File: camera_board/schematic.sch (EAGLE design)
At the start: 1 part

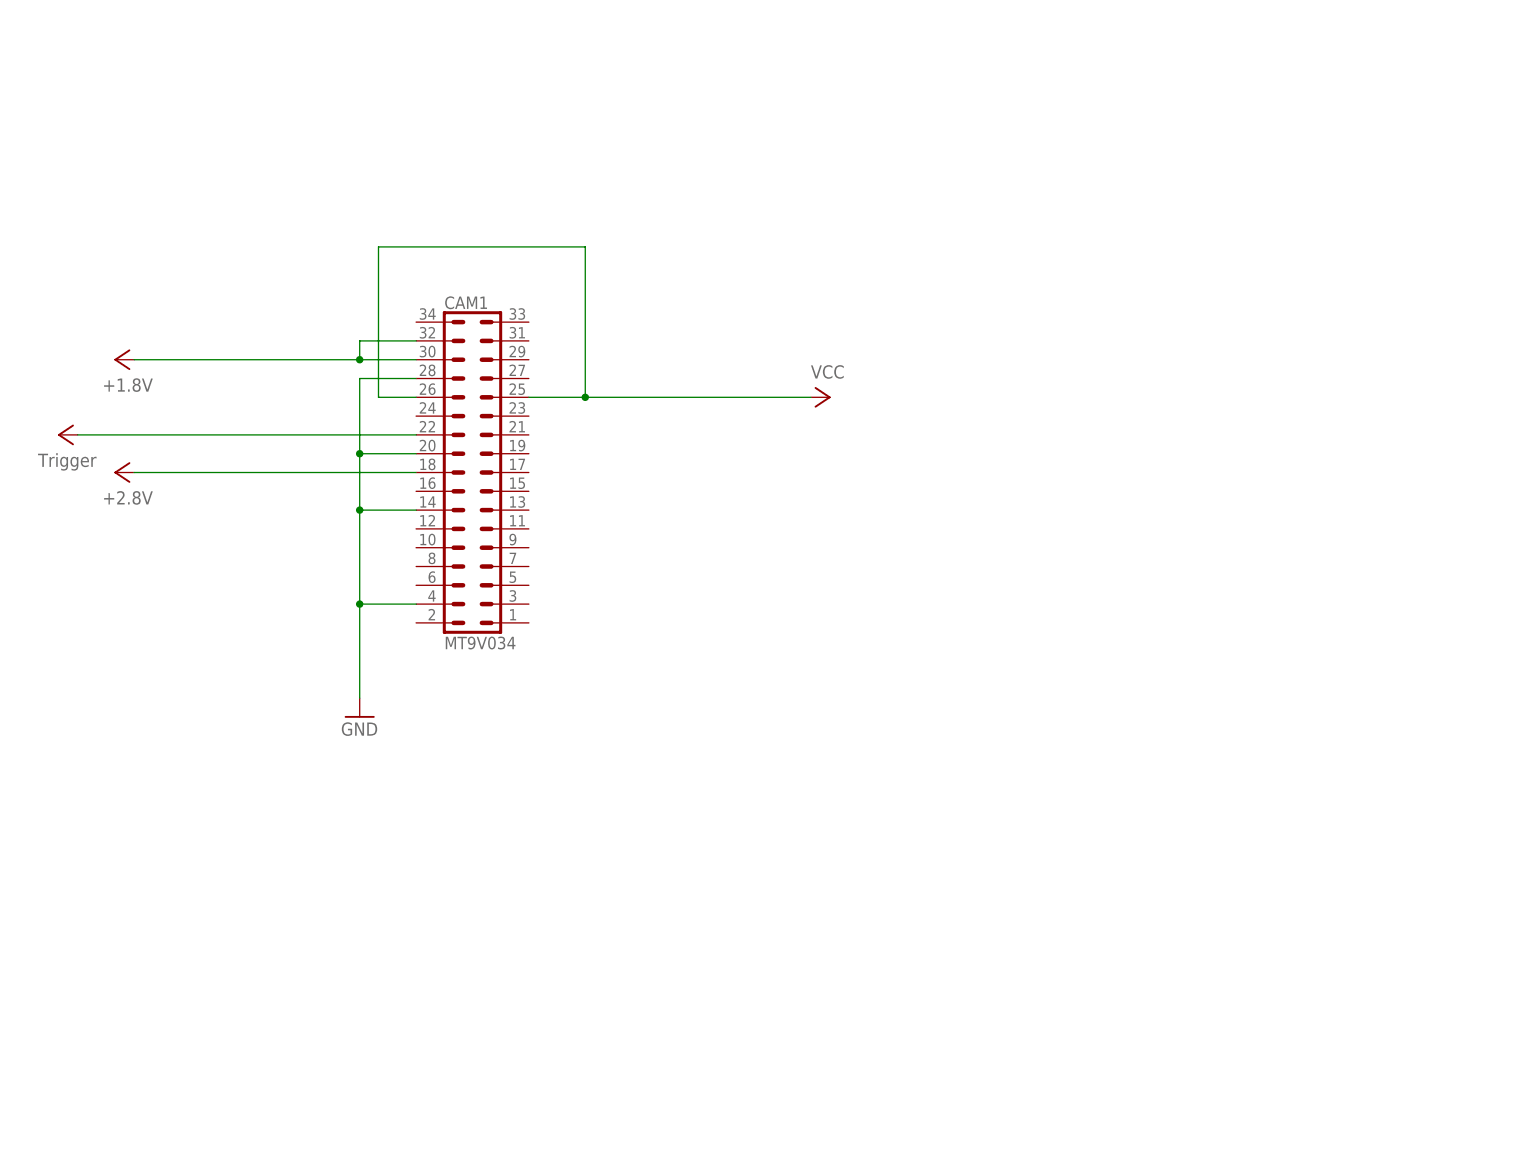
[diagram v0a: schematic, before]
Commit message: Completed Schematic, Started Board
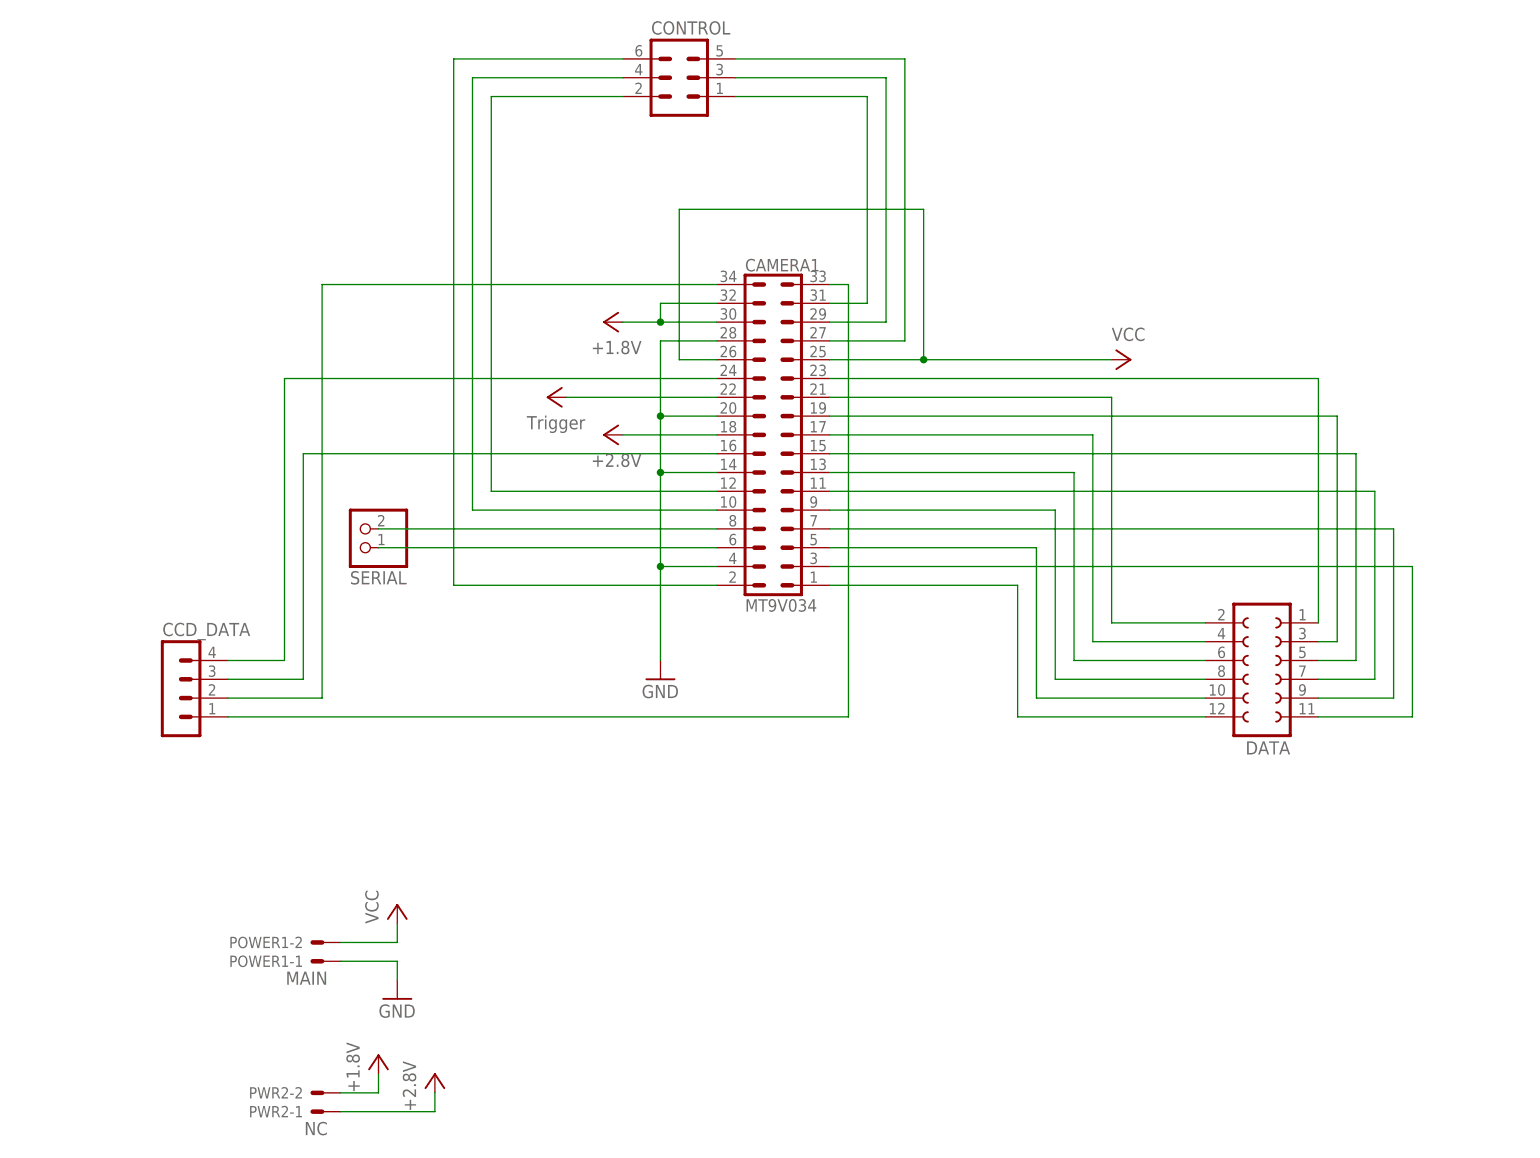
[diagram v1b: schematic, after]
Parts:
- removed CAM1: MT9V034, _hhn_con_pinhead_box_1mm27:PHB_1MM27_2X17_SNT
- added CAMERA1: MT9V034, _hhn_con_pinhead_box_1mm27:PHB_1MM27_2X17_SNT
- added CCD_DATA: (no value), con-lstb:MA04-1
- added CONTROL: (no value), con-lstb:MA03-2
- added DATA: (no value), con-lsta:FE06-2
- added POWER1: MAIN, con-molex:22-23-2021
- added PWR2: NC, con-molex:22-23-2021
- added SERIAL: (no value), pinhead:PINHD-1X2
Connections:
- new net N$1: CAMERA1.23, DATA.1
- new net N$10: CAMERA1.5, DATA.10
- new net N$11: CAMERA1.3, DATA.11
- new net N$12: CAMERA1.1, DATA.12
- new net N$13: CAMERA1.12, CONTROL.2
- new net N$14: CAMERA1.10, CONTROL.4
- new net N$15: CAMERA1.2, CONTROL.6
- new net N$16: CAMERA1.31, CONTROL.1
- new net N$17: CAMERA1.29, CONTROL.3
- new net N$18: CAMERA1.27, CONTROL.5
- new net N$19: CAMERA1.33, CCD_DATA.1
- new net N$2: CAMERA1.21, DATA.2
- new net N$20: CAMERA1.34, CCD_DATA.2
- new net N$21: CAMERA1.16, CCD_DATA.3
- new net N$22: CAMERA1.24, CCD_DATA.4
- new net N$23: CAMERA1.8, SERIAL.2
- new net N$24: CAMERA1.6, SERIAL.1
- new net N$3: CAMERA1.19, DATA.3
- new net N$4: CAMERA1.17, DATA.4
- new net N$5: CAMERA1.15, DATA.5
- new net N$6: CAMERA1.13, DATA.6
- new net N$7: CAMERA1.11, DATA.7
- new net N$8: CAMERA1.9, DATA.8
- new net N$9: CAMERA1.7, DATA.9
- net 1.8V: now also CAMERA1.30, CAMERA1.32, PWR2-2.S; no longer CAM1.30, CAM1.32
- net 2.8V: now also CAMERA1.18, PWR2-1.S; no longer CAM1.18
- net GND: now also CAMERA1.14, CAMERA1.20, CAMERA1.28, CAMERA1.4, POWER1-1.S; no longer CAM1.14, CAM1.20, CAM1.28, CAM1.4
- net TRIGGER: now also CAMERA1.22; no longer CAM1.22
- net VCC: now also CAMERA1.25, CAMERA1.26, POWER1-2.S; no longer CAM1.25, CAM1.26

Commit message: Updated Schematic and Board
I'm debating on removing the ccd_data pin breakout all together - more
to come on this
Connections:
- net N$13: now also CONTROL.6; no longer CONTROL.2
- net N$15: now also CONTROL.2; no longer CONTROL.6
- net N$16: now also CONTROL.5; no longer CONTROL.1
- net N$18: now also CONTROL.1; no longer CONTROL.5
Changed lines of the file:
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@@
 <pinref part="CAMERA1" gate="G$1" pin="12"/>
 <wire x1="116.84" y1="104.14" x2="86.36" y2="104.14" width="0.1524" layer="91"/>
-<wire x1="86.36" y1="104.14" x2="86.36" y2="157.48" width="0.1524" layer="91"/>
-<pinref part="CONTROL" gate="1" pin="2"/>
-<wire x1="86.36" y1="157.48" x2="104.14" y2="157.48" width="0.1524" layer="91"/>
+<wire x1="86.36" y1="104.14" x2="86.36" y2="162.56" width="0.1524" layer="91"/>
+<pinref part="CONTROL" gate="1" pin="6"/>
+<wire x1="86.36" y1="162.56" x2="104.14" y2="162.56" width="0.1524" layer="91"/>
 </segment>
 </net>
@@
 <pinref part="CAMERA1" gate="G$1" pin="2"/>
 <wire x1="116.84" y1="91.44" x2="81.28" y2="91.44" width="0.1524" layer="91"/>
-<wire x1="81.28" y1="91.44" x2="81.28" y2="162.56" width="0.1524" layer="91"/>
-<pinref part="CONTROL" gate="1" pin="6"/>
-<wire x1="81.28" y1="162.56" x2="104.14" y2="162.56" width="0.1524" layer="91"/>
+<wire x1="81.28" y1="91.44" x2="81.28" y2="157.48" width="0.1524" layer="91"/>
+<pinref part="CONTROL" gate="1" pin="2"/>
+<wire x1="81.28" y1="157.48" x2="104.14" y2="157.48" width="0.1524" layer="91"/>
 </segment>
 </net>
@@
 <pinref part="CAMERA1" gate="G$1" pin="31"/>
 <wire x1="132.08" y1="129.54" x2="137.16" y2="129.54" width="0.1524" layer="91"/>
-<wire x1="137.16" y1="129.54" x2="137.16" y2="157.48" width="0.1524" layer="91"/>
-<pinref part="CONTROL" gate="1" pin="1"/>
-<wire x1="137.16" y1="157.48" x2="119.38" y2="157.48" width="0.1524" layer="91"/>
+<wire x1="137.16" y1="129.54" x2="137.16" y2="162.56" width="0.1524" layer="91"/>
+<pinref part="CONTROL" gate="1" pin="5"/>
+<wire x1="119.38" y1="162.56" x2="137.16" y2="162.56" width="0.1524" layer="91"/>
 </segment>
 </net>
@@
 <pinref part="CAMERA1" gate="G$1" pin="27"/>
 <wire x1="132.08" y1="124.46" x2="142.24" y2="124.46" width="0.1524" layer="91"/>
-<wire x1="142.24" y1="124.46" x2="142.24" y2="162.56" width="0.1524" layer="91"/>
-<pinref part="CONTROL" gate="1" pin="5"/>
-<wire x1="142.24" y1="162.56" x2="119.38" y2="162.56" width="0.1524" layer="91"/>
+<wire x1="142.24" y1="124.46" x2="142.24" y2="157.48" width="0.1524" layer="91"/>
+<pinref part="CONTROL" gate="1" pin="1"/>
+<wire x1="119.38" y1="157.48" x2="142.24" y2="157.48" width="0.1524" layer="91"/>
 </segment>
 </net>

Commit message: Final Schematic
- Removed CCD_DATA lines, we can bodge these 4 pins if we end up needing
them but they don't appear connected in the LI-VM34LP schematic.

- Finished overall board design, added some extra text and moved around
labels so that everything comes out looking good
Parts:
- removed CCD_DATA: (no value), con-lstb:MA04-1
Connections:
- net N$19: no longer CCD_DATA.1
- net N$20: no longer CCD_DATA.2
- net N$21: no longer CCD_DATA.3
- net N$22: no longer CCD_DATA.4
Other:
- note added: "CCD_Data pins left unconnected"
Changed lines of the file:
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@@
 <part name="P+6" library="supply1" deviceset="+5V" device="" value="+2.8V"/>
 <part name="CONTROL" library="con-lstb" deviceset="MA03-2" device=""/>
-<part name="CCD_DATA" library="con-lstb" deviceset="MA04-1" device=""/>
 <part name="SERIAL" library="pinhead" deviceset="PINHD-1X2" device=""/>
 </parts>
@@
 <sheet>
 <plain>
+<text x="48.26" y="71.12" size="1.778" layer="91">CCD_Data pins left
+unconnected</text>
 </plain>
 <instances>
@@
 <instance part="P+6" gate="1" x="78.74" y="25.4"/>
 <instance part="CONTROL" gate="1" x="111.76" y="160.02"/>
-<instance part="CCD_DATA" gate="1" x="43.18" y="78.74"/>
 <instance part="SERIAL" gate="G$1" x="68.58" y="99.06" rot="R180"/>
 </instances>
@@
 <wire x1="132.08" y1="132.08" x2="134.62" y2="132.08" width="0.1524" layer="91"/>
 <wire x1="134.62" y1="132.08" x2="134.62" y2="73.66" width="0.1524" layer="91"/>
-<wire x1="134.62" y1="73.66" x2="50.8" y2="73.66" width="0.1524" layer="91"/>
-<pinref part="CCD_DATA" gate="1" pin="1"/>
+<wire x1="134.62" y1="73.66" x2="76.2" y2="73.66" width="0.1524" layer="91"/>
 </segment>
 </net>
 <net name="N$20" class="0">
 <segment>
-<pinref part="CCD_DATA" gate="1" pin="2"/>
-<wire x1="50.8" y1="76.2" x2="63.5" y2="76.2" width="0.1524" layer="91"/>
 <wire x1="63.5" y1="76.2" x2="63.5" y2="132.08" width="0.1524" layer="91"/>
 <pinref part="CAMERA1" gate="G$1" pin="34"/>
@@
 <wire x1="116.84" y1="109.22" x2="60.96" y2="109.22" width="0.1524" layer="91"/>
 <wire x1="60.96" y1="109.22" x2="60.96" y2="78.74" width="0.1524" layer="91"/>
-<pinref part="CCD_DATA" gate="1" pin="3"/>
-<wire x1="60.96" y1="78.74" x2="50.8" y2="78.74" width="0.1524" layer="91"/>
 </segment>
 </net>
@@
 <wire x1="116.84" y1="119.38" x2="58.42" y2="119.38" width="0.1524" layer="91"/>
 <wire x1="58.42" y1="119.38" x2="58.42" y2="81.28" width="0.1524" layer="91"/>
-<pinref part="CCD_DATA" gate="1" pin="4"/>
-<wire x1="58.42" y1="81.28" x2="50.8" y2="81.28" width="0.1524" layer="91"/>
 </segment>
 </net>
@@
 </schematic>
 </drawing>
+<compatibility>
+<note version="6.3" minversion="6.2.2" severity="warning">
+Since Version 6.2.2 text objects can contain more than one line,
+which will not be processed correctly with this version.
+</note>
+</compatibility>
 </eagle>

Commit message: Final Schematic Part II
Need to double check and then I'll order boards
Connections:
- removed net N$19: CAMERA1.33
- removed net N$20: CAMERA1.34
- removed net N$21: CAMERA1.16
- removed net N$22: CAMERA1.24
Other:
- moved on the sheet: CAMERA1, CONTROL, DATA, POWER1-1, POWER1-2, PWR2-1, PWR2-2, SERIAL

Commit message: Added missing pin, finalized(?) board design
- Missed the trigger pin, that could have been bad!
- Double checked the layout and it looks correct
- Passed OSHpark DRC, ERC
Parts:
- added TRIG: (no value), pinhead:PINHD-1X1
- renumbered POWER1 to POWER
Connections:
- net TRIGGER: now also TRIG.1
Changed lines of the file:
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@@
 <part name="TRIGGER" library="supply1" deviceset="+5V" device="" value="Trigger"/>
 <part name="DATA" library="con-lsta" deviceset="FE06-2" device=""/>
-<part name="POWER1" library="con-molex" deviceset="22-23-2021" device="" value="MAIN"/>
+<part name="POWER" library="con-molex" deviceset="22-23-2021" device="" value="MAIN"/>
 <part name="PWR2" library="con-molex" deviceset="22-23-2021" device="" value="NC"/>
 <part name="GND2" library="supply1" deviceset="GND" device=""/>
@@
 <part name="CONTROL" library="con-lstb" deviceset="MA03-2" device=""/>
 <part name="SERIAL" library="pinhead" deviceset="PINHD-1X2" device=""/>
+<part name="TRIGGER1" library="supply1" deviceset="+5V" device="" value="Trigger"/>
+<part name="TRIG" library="pinhead" deviceset="PINHD-1X1" device=""/>
 </parts>
 <sheets>
@@
 <instance part="TRIGGER" gate="1" x="109.22" y="109.22" rot="R90"/>
 <instance part="DATA" gate="G$1" x="205.74" y="73.66" rot="R180"/>
-<instance part="POWER1" gate="-1" x="48.26" y="129.54" rot="R180"/>
-<instance part="POWER1" gate="-2" x="48.26" y="132.08" rot="R180"/>
+<instance part="POWER" gate="-1" x="48.26" y="129.54" rot="R180"/>
+<instance part="POWER" gate="-2" x="48.26" y="132.08" rot="R180"/>
 <instance part="PWR2" gate="-1" x="48.26" y="109.22" rot="R180"/>
 <instance part="PWR2" gate="-2" x="48.26" y="111.76" rot="R180"/>
@@
 <instance part="CONTROL" gate="1" x="127" y="152.4"/>
 <instance part="SERIAL" gate="G$1" x="83.82" y="91.44" rot="R180"/>
+<instance part="TRIGGER1" gate="1" x="66.04" y="154.94" rot="R270"/>
+<instance part="TRIG" gate="G$1" x="35.56" y="154.94" rot="R180"/>
 </instances>
 <busses>
@@
 </segment>
 <segment>
-<pinref part="POWER1" gate="-2" pin="S"/>
+<pinref part="POWER" gate="-2" pin="S"/>
 <pinref part="P+4" gate="VCC" pin="VCC"/>
 <wire x1="50.8" y1="132.08" x2="58.42" y2="132.08" width="0.1524" layer="91"/>
@@
 </segment>
 <segment>
-<pinref part="POWER1" gate="-1" pin="S"/>
+<pinref part="POWER" gate="-1" pin="S"/>
 <pinref part="GND2" gate="1" pin="GND"/>
 <wire x1="50.8" y1="129.54" x2="58.42" y2="129.54" width="0.1524" layer="91"/>
@@
 <wire x1="111.76" y1="109.22" x2="132.08" y2="109.22" width="0.1524" layer="91"/>
 </segment>
+<segment>
+<pinref part="TRIG" gate="G$1" pin="1"/>
+<pinref part="TRIGGER1" gate="1" pin="+5V"/>
+<wire x1="38.1" y1="154.94" x2="63.5" y2="154.94" width="0.1524" layer="91"/>
+</segment>
 </net>
